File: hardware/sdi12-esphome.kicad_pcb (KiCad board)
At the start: 2 copper layers, 92.8 x 74 mm, 27 parts, among them J1 SDI-12 A, J2 SDI-12 B, J3 SDI-12 C, J4 SDI-12 D, Q1 2N7002, U1 ESP32_NODEMCU, U2 74LVC1G125, U3 MCP1661

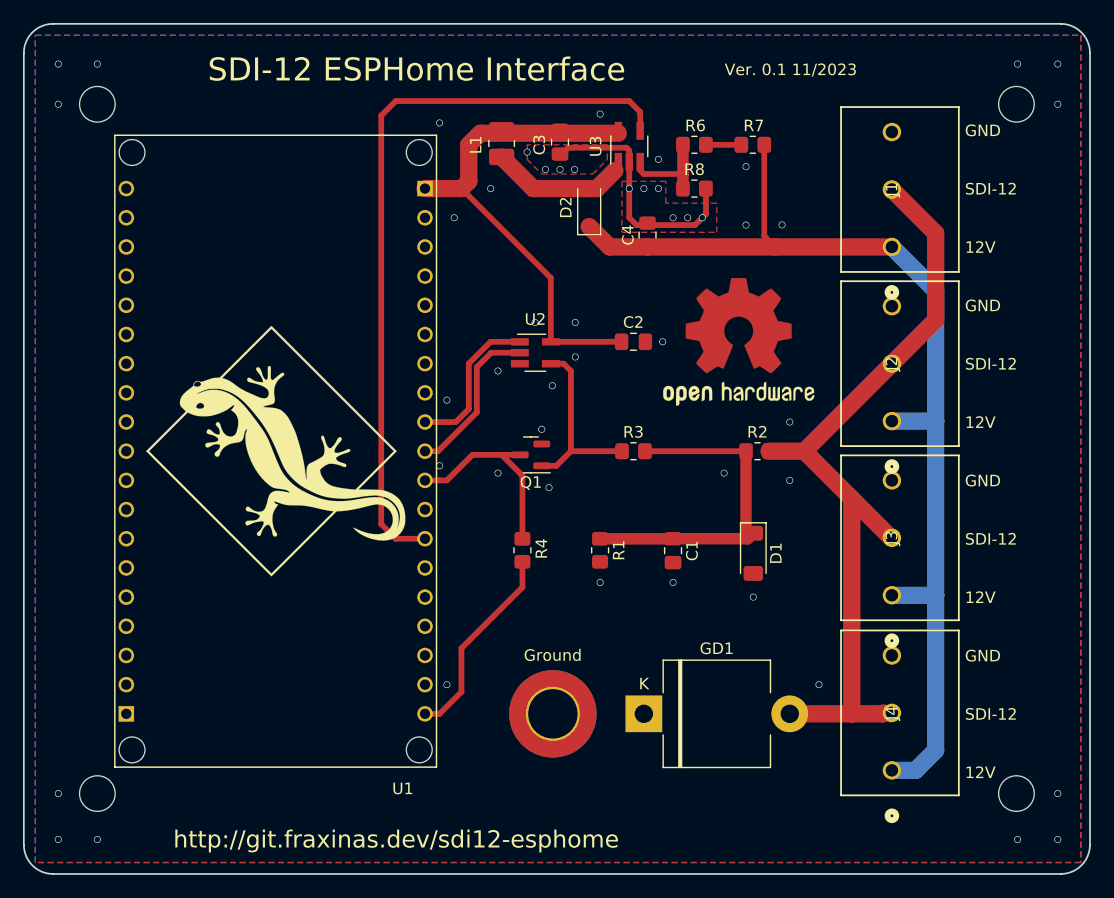
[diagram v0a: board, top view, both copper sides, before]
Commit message: board: Add additional GPIO and Rain Gauge ports, re-arrange PCB elements
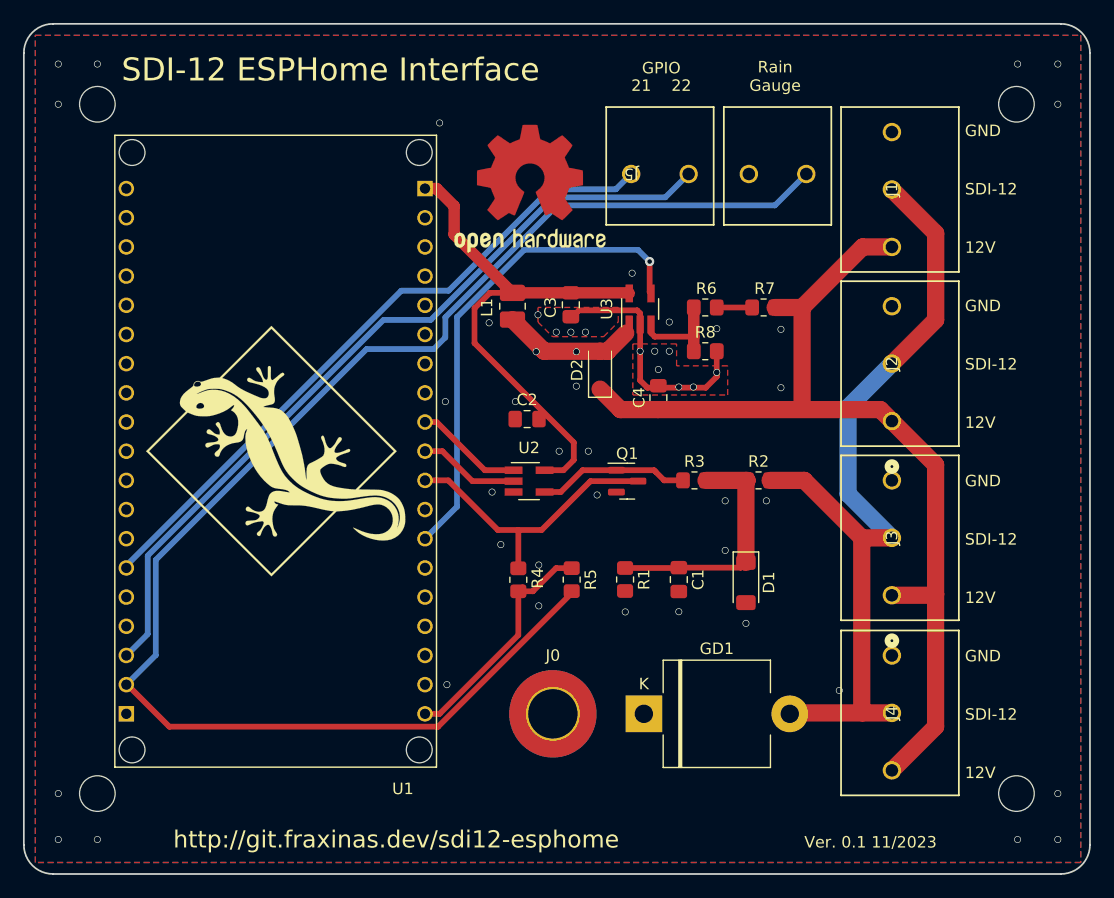
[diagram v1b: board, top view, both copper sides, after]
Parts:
- added J5: GPIO21/22, Fraxinas-kicad:Phoenix Contact SPTA 1 2 5,0 1752214, F.Cu at (96.9, 52.1)
- added J6: Rain Gauge, Fraxinas-kicad:Phoenix Contact SPTA 1 2 5,0 1752214, F.Cu at (107.1, 52.1)
- added R5: 4K7, Resistor_SMD:R_0805_2012Metric_Pad1.20x1.40mm_HandSolder, F.Cu at (86.7, 87.4)
- J1: footprint Fraxinas-kicad:Phoenix Contact SPTA 1 3 3,5 1752227 -> Fraxinas-kicad:Phoenix Contact SPTA 1 3 5,0 1752227
- moved LOGO1 22.5 mm to (83.1, 53.3)
- moved C3 14.2 mm to (86.6, 63.5)
- moved L1 14.2 mm to (81.5, 63.6)
- moved R6 14.2 mm to (98.3, 63.7)
- moved R7 14.2 mm to (103.4, 63.7)
- moved R8 14.2 mm to (98.3, 67.5)
- moved U3 14.2 mm to (92.6, 63.8)
- moved C4 14.2 mm to (94.2, 71.5)
- moved D2 14.2 mm to (89.2, 69.1)
- moved C2 11.4 mm to (82.8, 73.4)
- moved U2 11.2 mm to (83.0, 78.8)
- moved Q1 8.68 mm to (91.5, 78.8), turned to 0 degrees
- moved R3 5.89 mm to (97.4, 78.7)
- moved R1 3.34 mm to (91.3, 87.4)
- moved D1 2.62 mm to (101.9, 87.6)
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- renumbered Ground to J0
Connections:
- net Sender Enabled renamed OE
- C2 pad 1: +5V -> GND
- C2 pad 2: GND -> +5V
- GD1 pad 2: SDI12_Bus -> (no net)
- U1 pad J4_2: unconnected-(U1-G23-PadJ4_2) -> GPIO23
- U1 pad J4_3: unconnected-(U1-G22-PadJ4_3) -> GPIO22
- U1 pad J4_6: unconnected-(U1-G21-PadJ4_6) -> GPIO21
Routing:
- net GPIO23: track 0.00 -> 128.8 mm
- net GPIO22: track 0.00 -> 70.3 mm
- net GPIO21: track 0.00 -> 58.3 mm
- net VCC Enable: track 65.0 -> 42.9 mm, vias 0 -> 1
- net +12V: track 93.9 -> 85.1 mm
- net Net-(D1-K): track 30.2 -> 21.5 mm
- net RXD: track 17.3 -> 25.4 mm
- net TXD: track 14.1 -> 8.79 mm
- net OE: track 13.7 -> 9.72 mm
- net Net-(Q1-G): track 16.5 -> 13.2 mm
- net +3V3: track 17.5 -> 20.8 mm
- net +5V: track 43.4 -> 46.6 mm
- net SDI12_Bus: track 70.7 -> 73.4 mm
- net GND: vias 49 -> 50
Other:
- board text added: "21 22"
- board text added: "GPIO"
- board text added: "Rain Gauge"
